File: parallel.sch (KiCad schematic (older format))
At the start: 1 part

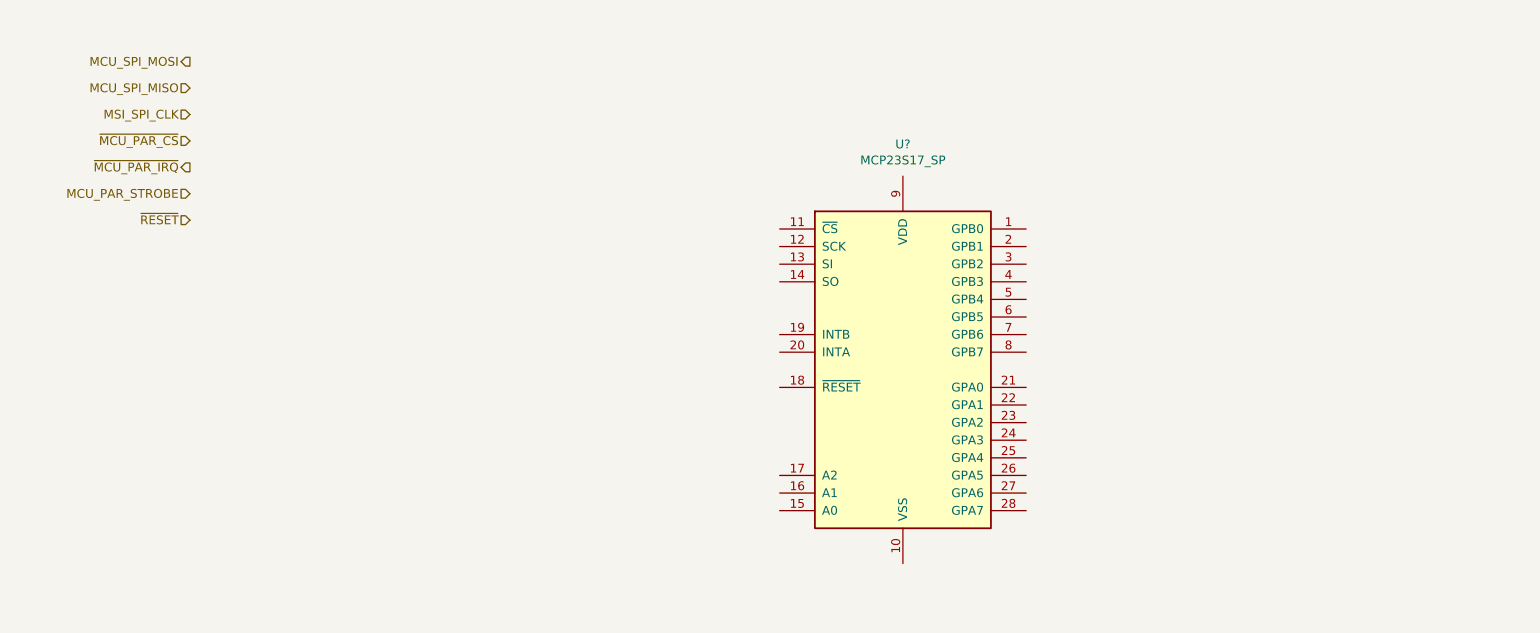
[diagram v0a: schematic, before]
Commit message: Added some footprints. Basic board outline.
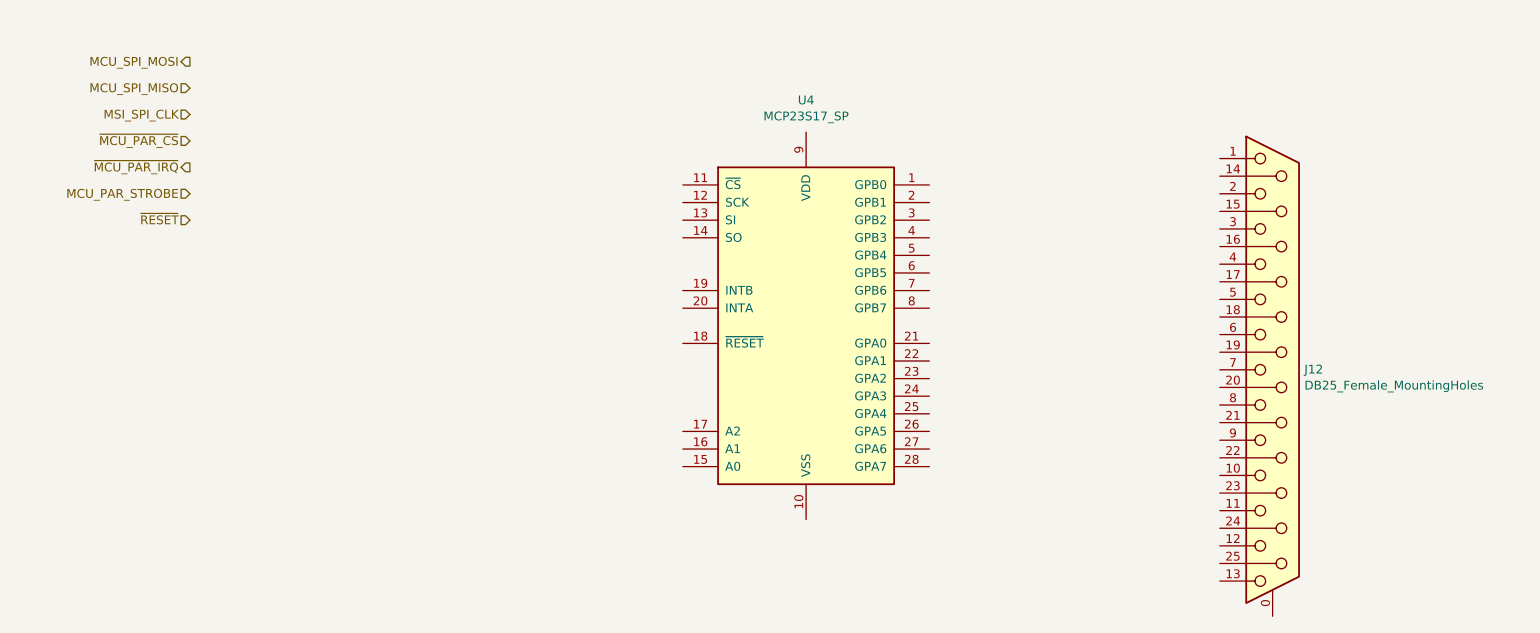
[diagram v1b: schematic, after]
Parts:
- added J12: DB25_Female_MountingHoles, Connector_Dsub:DSUB-25_Male_Horizontal_P2.77x2.84mm_EdgePinOffset4.94mm_Housed_MountingHolesOffset7.48mm, symbol Connector:DB25_Female_MountingHoles
- gave numbers to parts that had none: 1
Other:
- moved on the sheet: U4
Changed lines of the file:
@@
 $Descr A4 11693 8268
 encoding utf-8
-Sheet 9 11
+Sheet 8 11
 Title "Neotron 32K"
 Date "2019-12-08"
@@
 L Interface_Expansion:MCP23S17_SP U?
 U 1 1 5DF645A5
-P 6250 3700
+P 5700 3450
 AR Path="/5DF2345B/5DF645A5" Ref="U?"  Part="1"
-AR Path="/5DF626CD/5DF645A5" Ref="U?"  Part="1"
-F 0 "U?" H 6250 4981 50  0000 C CNN
-F 1 "MCP23S17_SP" H 6250 4890 50  0000 C CNN
-F 2 "Package_DIP:DIP-28_W7.62mm" H 6450 2700 50  0001 L CNN
-F 3 "http://ww1.microchip.com/downloads/en/DeviceDoc/20001952C.pdf" H 6450 2600 50  0001 L CNN
-	1    6250 3700
+AR Path="/5DF626CD/5DF645A5" Ref="U4"  Part="1"
+F 0 "U4" H 5700 4731 50  0000 C CNN
+F 1 "MCP23S17_SP" H 5700 4640 50  0000 C CNN
+F 2 "Package_DIP:DIP-28_W7.62mm" H 5900 2450 50  0001 L CNN
+F 3 "http://ww1.microchip.com/downloads/en/DeviceDoc/20001952C.pdf" H 5900 2350 50  0001 L CNN
+	1    5700 3450
 	1    0    0    -1
 $EndComp
@@
 Text HLabel 2200 2850 0    50   Input ~ 0
 ~RESET
+$Comp
+L Connector:DB25_Female_MountingHoles J12
+U 1 1 5E0F1D73
+P 8350 3700
+F 0 "J12" H 8530 3702 50  0000 L CNN
+F 1 "DB25_Female_MountingHoles" H 8530 3611 50  0000 L CNN
+F 2 "Connector_Dsub:DSUB-25_Male_Horizontal_P2.77x2.84mm_EdgePinOffset4.94mm_Housed_MountingHolesOffset7.48mm" H 8350 3700 50  0001 C CNN
+F 3 " ~" H 8350 3700 50  0001 C CNN
+	1    8350 3700
+	1    0    0    -1
+$EndComp
 $EndSCHEMATC

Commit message: Completed Power, SD, MIDI, Parallel and Joystick sheets.
Switch to sheet based 100x part numbering.
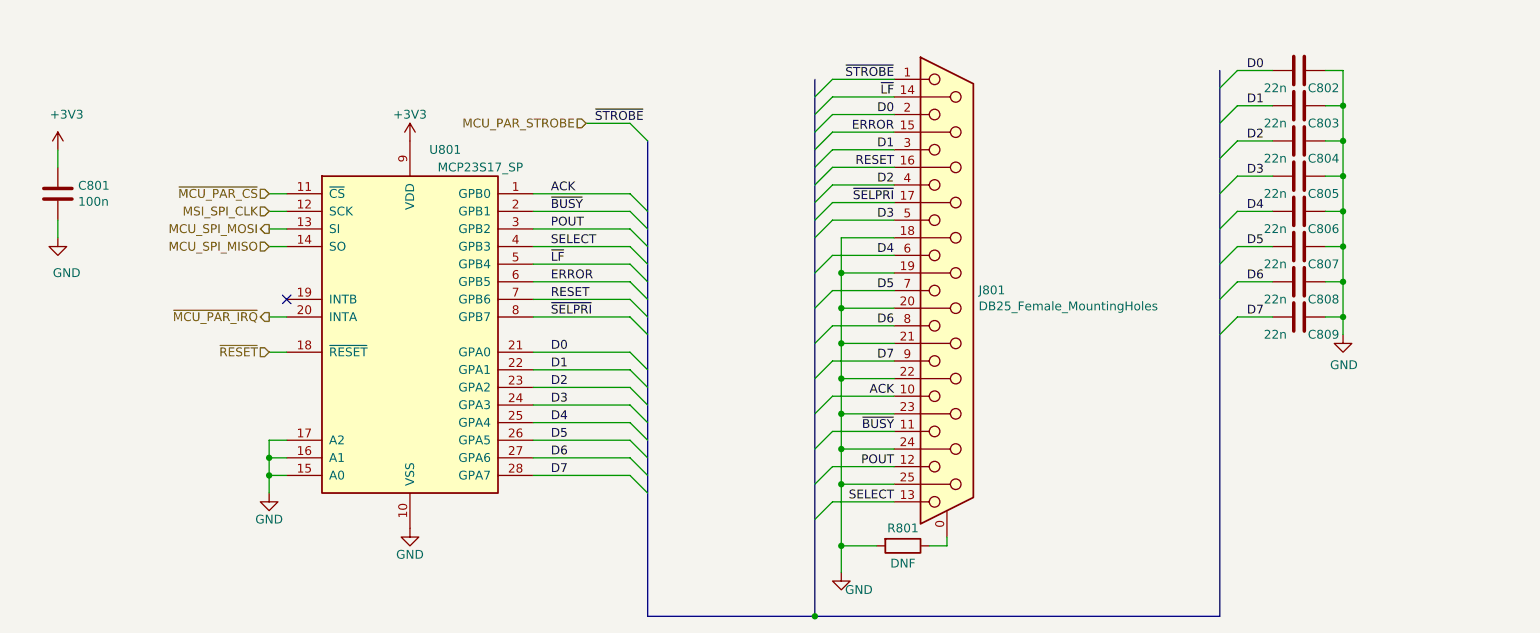
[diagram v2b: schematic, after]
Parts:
- removed U4: MCP23S17_SP, Package_DIP:DIP-28_W7.62mm, symbol Interface_Expansion:MCP23S17_SP
- added C801: 100n, Capacitor_THT:C_Disc_D3.0mm_W2.0mm_P2.50mm, symbol Device:C
- added C802, C803, C804, C805, C806, C807, C808, C809: 22n, Capacitor_THT:C_Disc_D3.0mm_W1.6mm_P2.50mm, symbol Device:C
- added R801: DNF, symbol Device:R
- added U801: MCP23S17_SP, Package_DIP:DIP-28_W7.62mm, symbol Interface_Expansion:MCP23S17_SP
- renumbered J12 to J801
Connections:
- net MCU_PAR_STROBE: now also J801.1
- net MCU_SPI_MISO: now also U801.14 (SO)
- net MCU_SPI_MOSI: now also U801.13 (SI)
- net MSI_SPI_CLK: now also U801.12 (SCK)
- net ~MCU_PAR_CS: now also U801.11 (~CS~)
- net ~MCU_PAR_IRQ: now also U801.20 (INTA)
- net ~RESET: now also U801.18 (~RESET~)
- net at J801.0 (PAD): now also R801.1
- net ACK: now reaches J801.10
- net ACK: now also U801.1 (GPB0)
- net ~BUSY: now reaches J801.11
- net ~BUSY: now also U801.2 (GPB1)
- net POUT: now reaches J801.12
- net POUT: now also U801.3 (GPB2)
- net SELECT: now reaches J801.13
- net SELECT: now also U801.4 (GPB3)
- net ~LF: now reaches J801.14 (P14)
- net ~LF: now also U801.5 (GPB4)
- net ERROR: now reaches J801.15 (P15)
- net ERROR: now also U801.6 (GPB5)
- net RESET: now reaches J801.16 (P16)
- net RESET: now also U801.7 (GPB6)
- net ~SELPRI: now reaches J801.17 (P17)
- net ~SELPRI: now also U801.8 (GPB7)
- net GND: now reaches J801.18 (P18)
- net GND: now also J801.19 (P19), J801.20 (P20), J801.21 (P21), J801.22 (P22), J801.23 (P23), J801.24 (P24), J801.25 (P25), C801.2, C802.1, C803.1, C804.1, C805.1, C806.1, C807.1, C808.1, C809.1, R801.2, U801.10 (VSS), U801.15 (A0), U801.16 (A1), U801.17 (A2)
- net D0: now reaches J801.2
- net D0: now also C802.2, U801.21 (GPA0)
- net D1: now reaches J801.3
- net D1: now also C803.2, U801.22 (GPA1)
- net D2: now reaches J801.4
- net D2: now also C804.2, U801.23 (GPA2)
- net D3: now reaches J801.5
- net D3: now also C805.2, U801.24 (GPA3)
- net D4: now reaches J801.6
- net D4: now also C806.2, U801.25 (GPA4)
- net D5: now reaches J801.7
- net D5: now also C807.2, U801.26 (GPA5)
- net D6: now reaches J801.8
- net D6: now also C808.2, U801.27 (GPA6)
- net D7: now reaches J801.9
- net D7: now also C809.2, U801.28 (GPA7)
- new net +3V3: C801.1, U801.9 (VDD)
- no-connect marks 0 -> 1
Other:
- moved on the sheet: J801

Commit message: Schematic capture draft complete.
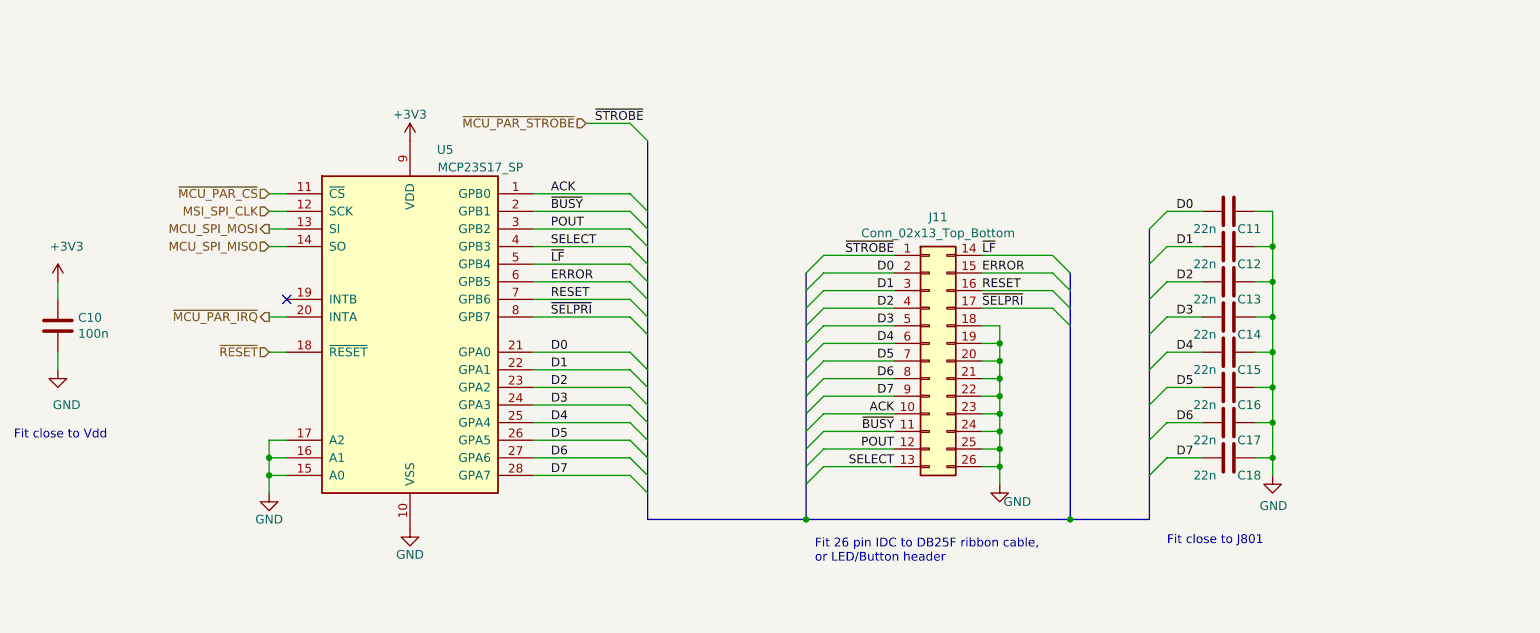
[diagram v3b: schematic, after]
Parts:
- removed J801: DB25_Female_MountingHoles, Connector_Dsub:DSUB-25_Male_Horizontal_P2.77x2.84mm_EdgePinOffset4.94mm_Housed_MountingHolesOffset7.48mm, symbol Connector:DB25_Female_MountingHoles
- removed R801: DNF, symbol Device:R
- added J11: Conn_02x13_Top_Bottom, Connector_PinHeader_2.54mm:PinHeader_2x13_P2.54mm_Vertical, symbol Connector_Generic:Conn_02x13_Top_Bottom
- C11: renamed from C802; footprint Capacitor_THT:C_Disc_D3.0mm_W1.6mm_P2.50mm -> Capacitor_THT:C_Disc_D3.0mm_W2.0mm_P2.50mm
- C12: renamed from C803; footprint Capacitor_THT:C_Disc_D3.0mm_W1.6mm_P2.50mm -> Capacitor_THT:C_Disc_D3.0mm_W2.0mm_P2.50mm
- C13: renamed from C804; footprint Capacitor_THT:C_Disc_D3.0mm_W1.6mm_P2.50mm -> Capacitor_THT:C_Disc_D3.0mm_W2.0mm_P2.50mm
- C14: renamed from C805; footprint Capacitor_THT:C_Disc_D3.0mm_W1.6mm_P2.50mm -> Capacitor_THT:C_Disc_D3.0mm_W2.0mm_P2.50mm
- C15: renamed from C806; footprint Capacitor_THT:C_Disc_D3.0mm_W1.6mm_P2.50mm -> Capacitor_THT:C_Disc_D3.0mm_W2.0mm_P2.50mm
- C16: renamed from C807; footprint Capacitor_THT:C_Disc_D3.0mm_W1.6mm_P2.50mm -> Capacitor_THT:C_Disc_D3.0mm_W2.0mm_P2.50mm
- C17: renamed from C808; footprint Capacitor_THT:C_Disc_D3.0mm_W1.6mm_P2.50mm -> Capacitor_THT:C_Disc_D3.0mm_W2.0mm_P2.50mm
- C18: renamed from C809; footprint Capacitor_THT:C_Disc_D3.0mm_W1.6mm_P2.50mm -> Capacitor_THT:C_Disc_D3.0mm_W2.0mm_P2.50mm
- renumbered C801 to C10, U801 to U5
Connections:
- net ACK: now also J11.10 (Pin_10)
- net D0: now also J11.2 (Pin_2)
- net D1: now also J11.3 (Pin_3)
- net D2: now also J11.4 (Pin_4)
- net D3: now also J11.5 (Pin_5)
- net D4: now also J11.6 (Pin_6)
- net D5: now also J11.7 (Pin_7)
- net D6: now also J11.8 (Pin_8)
- net D7: now also J11.9 (Pin_9)
- net ERROR: now also J11.15 (Pin_15)
- net GND: now also J11.18 (Pin_18), J11.19 (Pin_19), J11.20 (Pin_20), J11.21 (Pin_21), J11.22 (Pin_22), J11.23 (Pin_23), J11.24 (Pin_24), J11.25 (Pin_25), J11.26 (Pin_26)
- net POUT: now also J11.12 (Pin_12)
- net RESET: now also J11.16 (Pin_16)
- net SELECT: now also J11.13 (Pin_13)
- net ~BUSY: now also J11.11 (Pin_11)
- net ~LF: now also J11.14 (Pin_14)
- net ~SELPRI: now also J11.17 (Pin_17)
- new net ~MCU_PAR_STROBE: J11.1 (Pin_1)
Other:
- note added: "Fit 26 pin IDC to DB25F ribbon cable,\nor LED/Button header"
- note added: "Fit close to J801"
- note added: "Fit close to Vdd"
- moved on the sheet: C10, C11, C12, C13, C14, C15, C16, C17, C18

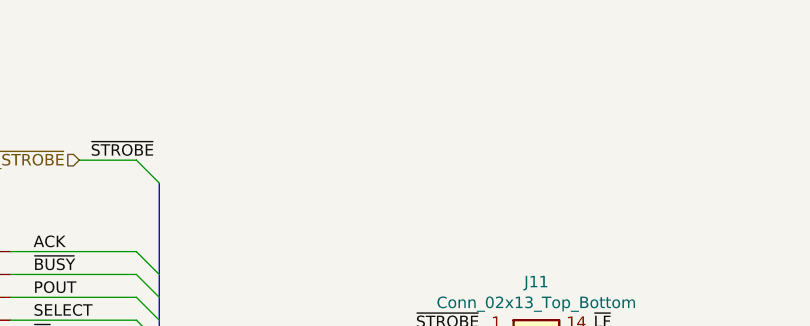
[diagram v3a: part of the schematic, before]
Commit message: Tidied up Atmega power. Added page titles.
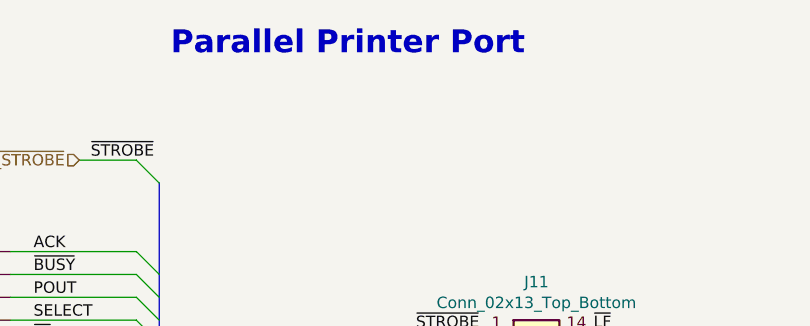
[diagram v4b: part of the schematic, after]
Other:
- note added: "Parallel Printer Port"
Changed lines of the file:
@@
 Sheet 6 10
 Title "Neotron 32K Main PCB"
-Date "2019-12-15"
-Rev "0.5"
+Date "2019-12-16"
+Rev "0.6"
 Comp "github.com/neotron-compute/Neotron-32-Hardware"
 Comment1 "Copyright (c) Jonathan 'theJPster' Pallant"
@@
 Text Label 4250 3400 0    50   ~ 0
 ~SELPRI
+Text Notes 4850 1850 0    100  ~ 20
+Parallel Printer Port
 Wire Bus Line
 	7200 3150 7200 4550
